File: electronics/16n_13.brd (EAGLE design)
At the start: 248.9 x 120.7 mm, 112 parts, among them J1 PJ302M, J10 PJ302M, J11 PJ302M, J12 PJ302M, J13 PJ302M, J14 PJ302M, J15 PJ302M, J16 PJ302M, J2 PJ302M, J3 PJ302M, J4 PJ302M, J5 PJ302M, J6 PJ302M, J7 PJ302M, J8 PJ302M, J9 PJ302M, U1 MCP6004_SMD, U2 MCP6004_SMD, U3 MCP6004_SMD, U4 MCP6004_SMD, U5 MCP6004_SMD, U6 MCP6004_SMD, U7 MCP6004_SMD, U8 MCP6004_SMD, U9 CD74HC4067SM96

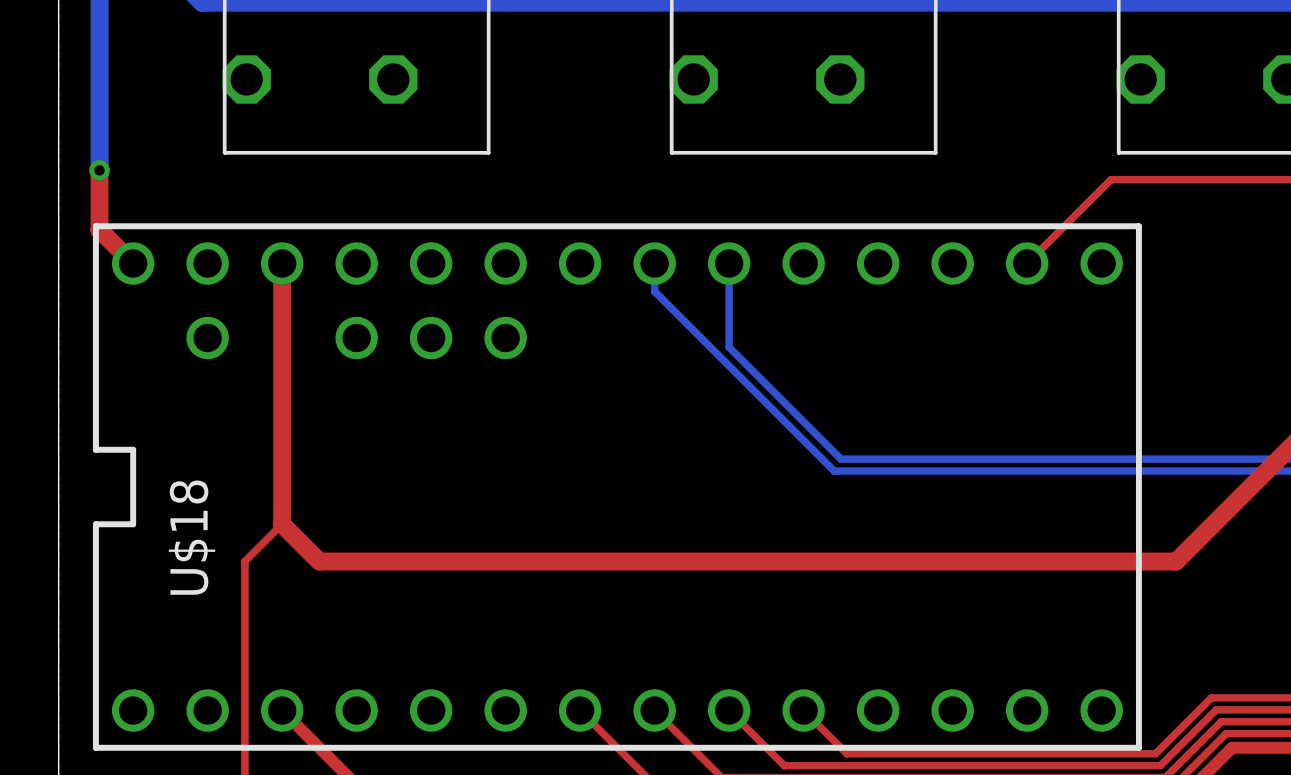
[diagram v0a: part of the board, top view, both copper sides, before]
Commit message: Given Teensy 3.2 AREF is 3.3V... let's strip out the inner pins.
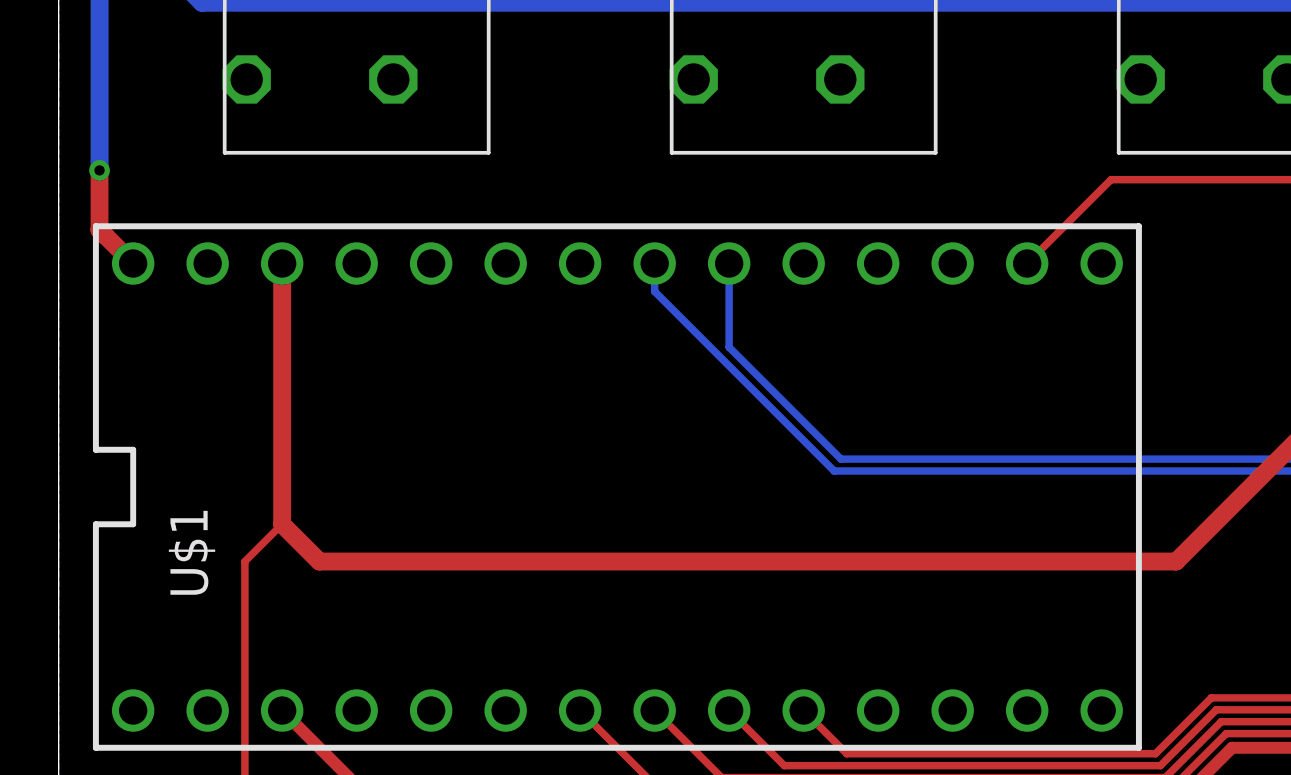
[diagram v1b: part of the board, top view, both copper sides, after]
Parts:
- removed U$18: TEENSY_3.1-3.2_DIL+4, Teensy_3_and_LC_Series_Boards_v1.4:TEENSY_3.0-3.2&LC_DIL+4
- added U$1: TEENSY_3.1-3.2_DIL, Teensy_3_and_LC_Series_Boards_v1.4:TEENSY_3.0-3.2&LC_DIL
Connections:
- removed net AREF: U$18.AREF
- removed net VUSB: U$18.VUSB
- net +3V3: now also U$1.3.3V; no longer U$18.3.3V
- net +5V: now also U$1.VIN; no longer U$18.VIN
- net ANALOG_IN: now also U$1.14/A0; no longer U$18.14/A0
- net GND: now also U$1.AGND, U$1.GND; no longer U$18.AGND, U$18.GND
- net MIDI_OUT: now also U$1.1; no longer U$18.1
- net S0: now also U$1.8; no longer U$18.8
- net S1: now also U$1.7; no longer U$18.7
- net S2: now also U$1.6; no longer U$18.6
- net S3: now also U$1.5; no longer U$18.5
- net SCL: now also U$1.19/A5; no longer U$18.19/A5
- net SDA: now also U$1.18/A4; no longer U$18.18/A4
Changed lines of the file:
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@@
 <attribute name="VALUE" x="65.7225" y="28.8925" size="1.27" layer="27" rot="R180"/>
 </element>
-<element name="U$18" library="Teensy_3_and_LC_Series_Boards_v1.4" package="TEENSY_3.0-3.2&amp;LC_DIL+4" value="TEENSY_3.1-3.2_DIL+4" x="19.05" y="14.605" rot="R90"/>
+<element name="U$1" library="Teensy_3_and_LC_Series_Boards_v1.4" package="TEENSY_3.0-3.2&amp;LC_DIL" value="TEENSY_3.1-3.2_DIL" x="19.05" y="14.605" rot="R90"/>
 </elements>
 <signals>
@@
 <contactref element="C9" pad="2"/>
 <via x="240.9825" y="7.3025" extent="1-16" drill="0.35"/>
-<contactref element="U$18" pad="GND"/>
-<contactref element="U$18" pad="AGND"/>
+<contactref element="U$1" pad="GND"/>
+<contactref element="U$1" pad="AGND"/>
 </signal>
 <signal name="+3V3">
@@
 <wire x1="56.1975" y1="24.3714" x2="63.5" y2="24.3714" width="0.254" layer="1"/>
 <wire x1="63.5" y1="24.3714" x2="68.0211" y2="24.3714" width="0.254" layer="1"/>
-<contactref element="U$18" pad="3.3V"/>
 <wire x1="7.62" y1="13.335" x2="6.35" y2="12.065" width="0.254" layer="1"/>
 <wire x1="6.35" y1="12.065" x2="6.35" y2="3.4925" width="0.254" layer="1"/>
@@
 <wire x1="68.0211" y1="24.3714" x2="68.8975" y2="23.495" width="0.254" layer="1"/>
 <wire x1="68.8975" y1="23.495" x2="71.9517" y2="23.495" width="0.254" layer="1"/>
-<wire x1="7.62" y1="22.225" x2="7.62" y2="13.335" width="0.6096" layer="1"/>
 <wire x1="7.62" y1="13.335" x2="8.89" y2="12.065" width="0.6096" layer="1"/>
 <wire x1="8.89" y1="12.065" x2="38.1" y2="12.065" width="0.6096" layer="1"/>
+<contactref element="U$1" pad="3.3V"/>
+<wire x1="7.62" y1="22.225" x2="7.62" y2="13.335" width="0.6096" layer="1"/>
 </signal>
 <signal name="A0">
@@
 <wire x1="1.3942" y1="25.4" x2="1.3942" y2="23.3708" width="0.6096" layer="1"/>
 <wire x1="1.3942" y1="23.3708" x2="1.5875" y2="23.1775" width="0.6096" layer="1"/>
-<contactref element="U$18" pad="VIN"/>
-<wire x1="1.3942" y1="23.3708" x2="2.54" y2="22.225" width="0.6096" layer="1"/>
+<contactref element="U$1" pad="VIN"/>
+<wire x1="2.54" y1="22.225" x2="1.5875" y2="23.1775" width="0.6096" layer="1"/>
 </signal>
 <signal name="N$3">
@@
 <wire x1="45.2555875" y1="6.5278" x2="44.4427875" y2="5.715" width="0.4064" layer="1"/>
 <wire x1="44.4427875" y1="5.715" x2="40.005" y2="5.715" width="0.4064" layer="1"/>
-<contactref element="U$18" pad="1"/>
+<wire x1="10.795" y1="3.81" x2="11.1125" y2="3.81" width="0.4064" layer="1"/>
+<contactref element="U$1" pad="1"/>
 <wire x1="7.62" y1="6.985" x2="10.795" y2="3.81" width="0.4064" layer="1"/>
-<wire x1="10.795" y1="3.81" x2="11.1125" y2="3.81" width="0.4064" layer="1"/>
 </signal>
 <signal name="N$1">
@@
 <wire x1="51.435" y1="16.03723125" x2="53.421115625" y2="14.051115625" width="0.4064" layer="1"/>
 <wire x1="53.421115625" y1="14.051115625" x2="55.4825" y2="11.98973125" width="0.4064" layer="1"/>
-<contactref element="U$18" pad="18/A4"/>
-<wire x1="22.86" y1="22.225" x2="22.86" y2="19.3675" width="0.254" layer="16"/>
-<wire x1="26.67" y1="15.5575" x2="22.86" y2="19.3675" width="0.254" layer="16"/>
+<wire x1="22.86" y1="19.3675" x2="26.67" y2="15.5575" width="0.254" layer="16"/>
 <wire x1="55.4825" y1="10.16" x2="55.4825" y2="10.08" width="0.254" layer="16"/>
 <wire x1="26.67" y1="15.5575" x2="44.45" y2="15.5575" width="0.254" layer="16"/>
@@
 <wire x1="53.895" y1="11.7475" x2="55.4825" y2="10.16" width="0.254" layer="16"/>
 <wire x1="48.26" y1="11.7475" x2="53.895" y2="11.7475" width="0.254" layer="16"/>
+<contactref element="U$1" pad="18/A4"/>
+<wire x1="22.86" y1="22.225" x2="22.86" y2="19.3675" width="0.254" layer="16"/>
 </signal>
 <signal name="SCL">
@@
 <wire x1="45.4825" y1="12.78" x2="48.895" y2="16.1925" width="0.4064" layer="1"/>
 <via x="48.895" y="18.415" extent="1-16" drill="0.35"/>
-<contactref element="U$18" pad="19/A5"/>
 <wire x1="45.4825" y1="10.08" x2="45.4825" y2="13.89" width="0.254" layer="16"/>
 <wire x1="45.4825" y1="13.89" x2="44.2214" y2="15.1511" width="0.254" layer="16"/>
-<wire x1="26.4414" y1="15.1511" x2="20.32" y2="21.2725" width="0.254" layer="16"/>
-<wire x1="20.32" y1="21.2725" x2="20.32" y2="22.225" width="0.254" layer="16"/>
+<wire x1="20.32" y1="21.2725" x2="26.4414" y2="15.1511" width="0.254" layer="16"/>
 <wire x1="44.2214" y1="15.1511" x2="26.4414" y2="15.1511" width="0.254" layer="16"/>
+<contactref element="U$1" pad="19/A5"/>
+<wire x1="20.32" y1="22.225" x2="20.32" y2="21.2725" width="0.254" layer="16"/>
 </signal>
 <signal name="W0">
@@
 </signal>
 <signal name="ANALOG_IN">
-<contactref element="U$18" pad="14/A0"/>
-<wire x1="33.02" y1="22.225" x2="33.97" y2="23.175" width="0.254" layer="1"/>
 <contactref element="U9" pad="1"/>
-<wire x1="33.97" y1="23.175" x2="33.97" y2="23.175" width="0.254" layer="1"/>
-<wire x1="33.97" y1="23.175" x2="35.8775" y2="25.0825" width="0.254" layer="1"/>
 <wire x1="35.8775" y1="25.0825" x2="60.0075" y2="25.0825" width="0.254" layer="1"/>
 <via x="60.0075" y="25.0825" extent="1-16" drill="0.35"/>
@@
 <via x="60.0075" y="23.495" extent="1-16" drill="0.35"/>
 <wire x1="60.0075" y1="23.495" x2="62.6683" y2="23.495" width="0.254" layer="1"/>
+<contactref element="U$1" pad="14/A0"/>
+<wire x1="33.02" y1="22.225" x2="35.8775" y2="25.0825" width="0.254" layer="1"/>
 </signal>
 <signal name="S0">
@@
 <wire x1="44.550675" y1="8.2296" x2="56.02224375" y2="8.2296" width="0.254" layer="1"/>
 <wire x1="43.737875" y1="7.4168" x2="44.550675" y2="8.2296" width="0.254" layer="1"/>
-<contactref element="U$18" pad="8"/>
-<wire x1="25.4" y1="6.985" x2="26.8732" y2="5.5118" width="0.254" layer="1"/>
 <wire x1="56.02224375" y1="8.2296" x2="59.85764375" y2="12.065" width="0.254" layer="1"/>
 <wire x1="59.85764375" y1="12.065" x2="62.6683" y2="12.065" width="0.254" layer="1"/>
+<contactref element="U$1" pad="8"/>
+<wire x1="25.4" y1="6.985" x2="26.8732" y2="5.5118" width="0.254" layer="1"/>
 </signal>
 <signal name="S1">
@@
 <wire x1="39.468425" y1="7.0104" x2="43.9062125" y2="7.0104" width="0.254" layer="1"/>
 <wire x1="56.19058125" y1="7.8232" x2="59.108690625" y2="10.741309375" width="0.254" layer="1"/>
-<contactref element="U$18" pad="7"/>
-<wire x1="22.86" y1="6.985" x2="24.7396" y2="5.1054" width="0.254" layer="1"/>
 <wire x1="62.6683" y1="10.795" x2="59.16238125" y2="10.795" width="0.254" layer="1"/>
 <wire x1="59.16238125" y1="10.795" x2="59.108690625" y2="10.741309375" width="0.254" layer="1"/>
+<contactref element="U$1" pad="7"/>
+<wire x1="22.86" y1="6.985" x2="24.7396" y2="5.1054" width="0.254" layer="1"/>
 </signal>
 <signal name="S2">
@@
 <wire x1="44.07455" y1="6.604" x2="44.88735" y2="7.4168" width="0.254" layer="1"/>
 <wire x1="44.88735" y1="7.4168" x2="64.6208375" y2="7.4168" width="0.254" layer="1"/>
-<contactref element="U$18" pad="6"/>
-<wire x1="20.32" y1="6.985" x2="22.606" y2="4.699" width="0.254" layer="1"/>
 <wire x1="22.606" y1="4.699" x2="37.7317625" y2="4.699" width="0.254" layer="1"/>
 <wire x1="71.9517" y1="10.795" x2="69.85" y2="10.795" width="0.254" layer="1"/>
@@
 <wire x1="69.215" y1="10.16" x2="69.215" y2="7.9375" width="0.254" layer="1"/>
 <wire x1="68.6689" y1="7.3914" x2="67.3989" y2="7.3914" width="0.254" layer="1"/>
+<contactref element="U$1" pad="6"/>
+<wire x1="20.32" y1="6.985" x2="22.606" y2="4.699" width="0.254" layer="1"/>
 </signal>
 <signal name="S3">
@@
 <wire x1="39.8051" y1="6.1976" x2="44.2428875" y2="6.1976" width="0.254" layer="1"/>
 <wire x1="45.0556875" y1="7.0104" x2="64.4525" y2="7.0104" width="0.254" layer="1"/>
-<contactref element="U$18" pad="5"/>
-<wire x1="17.78" y1="6.985" x2="20.4724" y2="4.2926" width="0.254" layer="1"/>
 <wire x1="20.4724" y1="4.2926" x2="20.6375" y2="4.2926" width="0.254" layer="1"/>
 <wire x1="67.6275" y1="6.985" x2="69.5325" y2="6.985" width="0.254" layer="1"/>
@@
 <wire x1="70.1675" y1="8.89" x2="70.8025" y2="9.525" width="0.254" layer="1"/>
 <wire x1="70.8025" y1="9.525" x2="71.9517" y2="9.525" width="0.254" layer="1"/>
-</signal>
-<signal name="VUSB">
-<contactref element="U$18" pad="VUSB"/>
-</signal>
-<signal name="AREF">
-<contactref element="U$18" pad="AREF"/>
+<contactref element="U$1" pad="5"/>
+<wire x1="17.78" y1="6.985" x2="20.4724" y2="4.2926" width="0.254" layer="1"/>
 </signal>
 </signals>

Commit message: Tidying and eyeballing layout.
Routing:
- net W1: track 108.8 -> 137.0 mm
- net N$301: track 111.6 -> 137.7 mm
- net N$302: track 108.1 -> 131.2 mm
- net W2: track 119.9 -> 140.9 mm
- net N$307: track 103.1 -> 119.1 mm
- net W7: track 97.4 -> 113.0 mm
- net W3: track 116.4 -> 131.7 mm
- net N$303: track 117.2 -> 132.5 mm
- net W6: track 114.9 -> 127.5 mm
- net N$304: track 114.9 -> 126.4 mm
- net N$306: track 99.8 -> 110.9 mm
- net W5: track 114.8 -> 124.3 mm
- net N$305: track 118.8 -> 127.7 mm
- net W9: track 93.2 -> 101.8 mm
- net N$309: track 95.2 -> 103.1 mm
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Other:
- board text added: "Teensy 3.2"
